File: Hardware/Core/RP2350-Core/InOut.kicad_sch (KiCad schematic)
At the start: 20 parts, among them CN10 PR5L4015-5P-C-F, CN11 PR5L4015-5P-C-F, CN7 PR5L4015-5P-C-F, CN8 PR5L4015-5P-C-F, CN9 PR5L4015-5P-C-F, J1 Conn_01x10_Socket, J2 Conn_01x10_Socket, J5 Conn_01x10_Socket, J6 Conn_01x10_Socket, J9 Conn_01x10_Socket, U35 PR5L5015-5P-C-H, U36 PR5L5015-5P-C-H, U37 PR5L5015-5P-C-H, U38 PR5L5015-5P-C-H, U39 PR5L5015-5P-C-H

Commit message: Verison RP2350 with arduino header support
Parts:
- removed J1, J2, J5, J6: Conn_01x10_Socket, Connector_PinHeader_2.54mm:PinHeader_2x10_P2.54mm_Vertical, symbol Connector:Conn_01x10_Socket
- J9: footprint Connector_PinHeader_2.54mm:PinHeader_2x10_P2.54mm_Vertical -> Connector_PinHeader_2.54mm:PinHeader_2x05_P2.54mm_Vertical
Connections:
- net ADC4_GPIO44 is gone; now on net SCL_ALT: A1.13 (SDA/A4)
- net ADC5_GPIO45 is gone; now on net SDA_ALT: A1.14 (SCL/A5)
- net GPIO25 is gone; now on net GPIO20: A1.24 (D9)
- net GPIO26 is gone; now on net GPIO21: A1.25 (D10)
- net GPIO27 is gone; now on net GPIO22: A1.26 (D11)
- net GPIO28 is gone; now on net GPIO23: A1.27 (D12)
- net GPIO29 is gone; now on net GPIO24: A1.28 (D13)
- net GPIO13: now also A1.19 (D4)
- net GPIO14: now also A1.20 (D5)
- net GPIO15: now also A1.21 (D6)
- net GPIO18: now also A1.22 (D7); no longer A1.17 (D2)
- net GPIO19: now also A1.23 (D8); no longer A1.18 (D3)
- net GPIO2: now also A1.17 (D2)
- net GPIO20: no longer A1.19 (D4)
- net GPIO21: no longer A1.20 (D5)
- net GPIO22: no longer A1.21 (D6)
- net GPIO23: no longer A1.22 (D7)
- net GPIO24: no longer A1.23 (D8)
- net GPIO4: now also A1.18 (D3)
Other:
- note added: "EXP HiSpeed"
- note removed: "EXP"
- moved on the sheet: J9

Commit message: Connectors connection improvements
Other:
- note added: "Only for RP235X-B"
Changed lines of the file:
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@@
+		)
+	)
+	(text "Only for RP235X-B"
+		(exclude_from_sim no)
+		(at 256.54 111.76 0)
+		(effects
+			(font
+				(size 2.54 2.54)
+			)
 		)
 	)

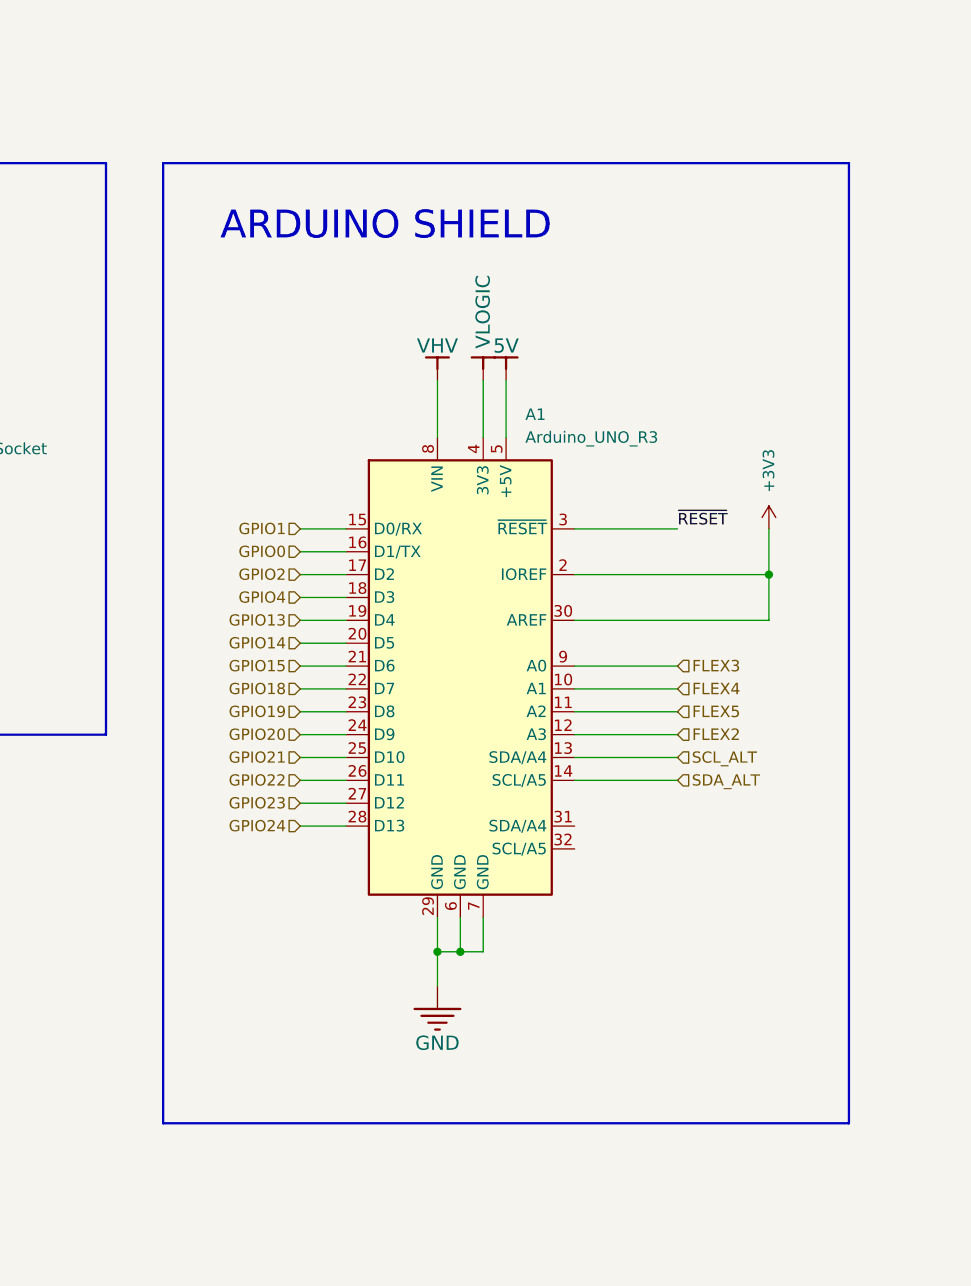
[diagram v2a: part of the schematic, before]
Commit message: Added ADC TI ADS1115IDGSR to match arduino pinout and function and isolate arduino connections from spaghetti bus
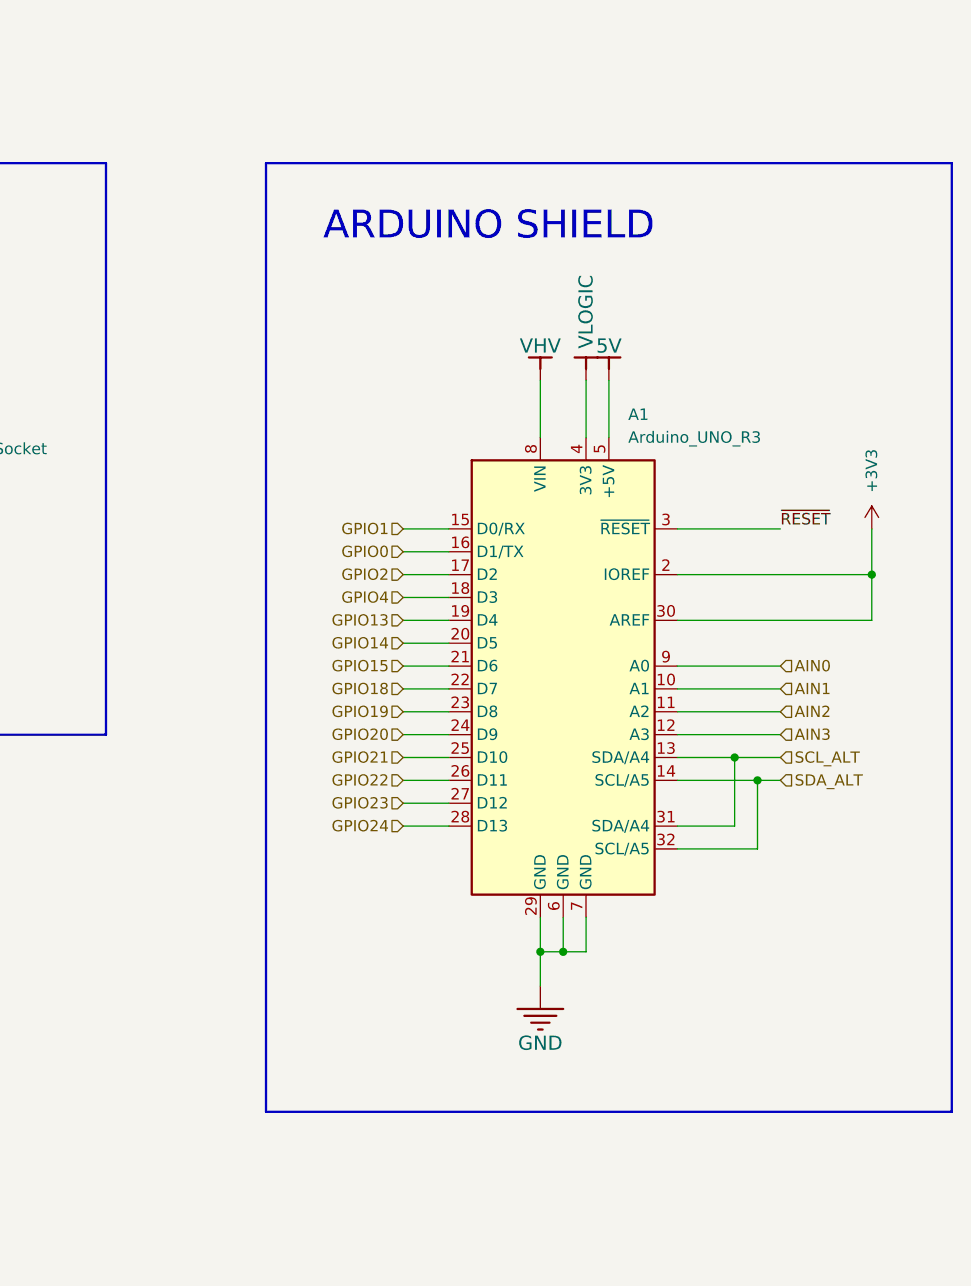
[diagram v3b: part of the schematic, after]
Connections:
- net FLEX2: no longer A1.12 (A3)
- net FLEX3: no longer A1.9 (A0)
- net FLEX4: no longer A1.10 (A1)
- net FLEX5: no longer A1.11 (A2)
- net SCL_ALT: now also A1.31 (SDA/A4)
- net SDA_ALT: now also A1.32 (SCL/A5)
- new net AIN0: A1.9 (A0)
- new net AIN1: A1.10 (A1)
- new net AIN2: A1.11 (A2)
- new net AIN3: A1.12 (A3)
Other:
- moved on the sheet: A1

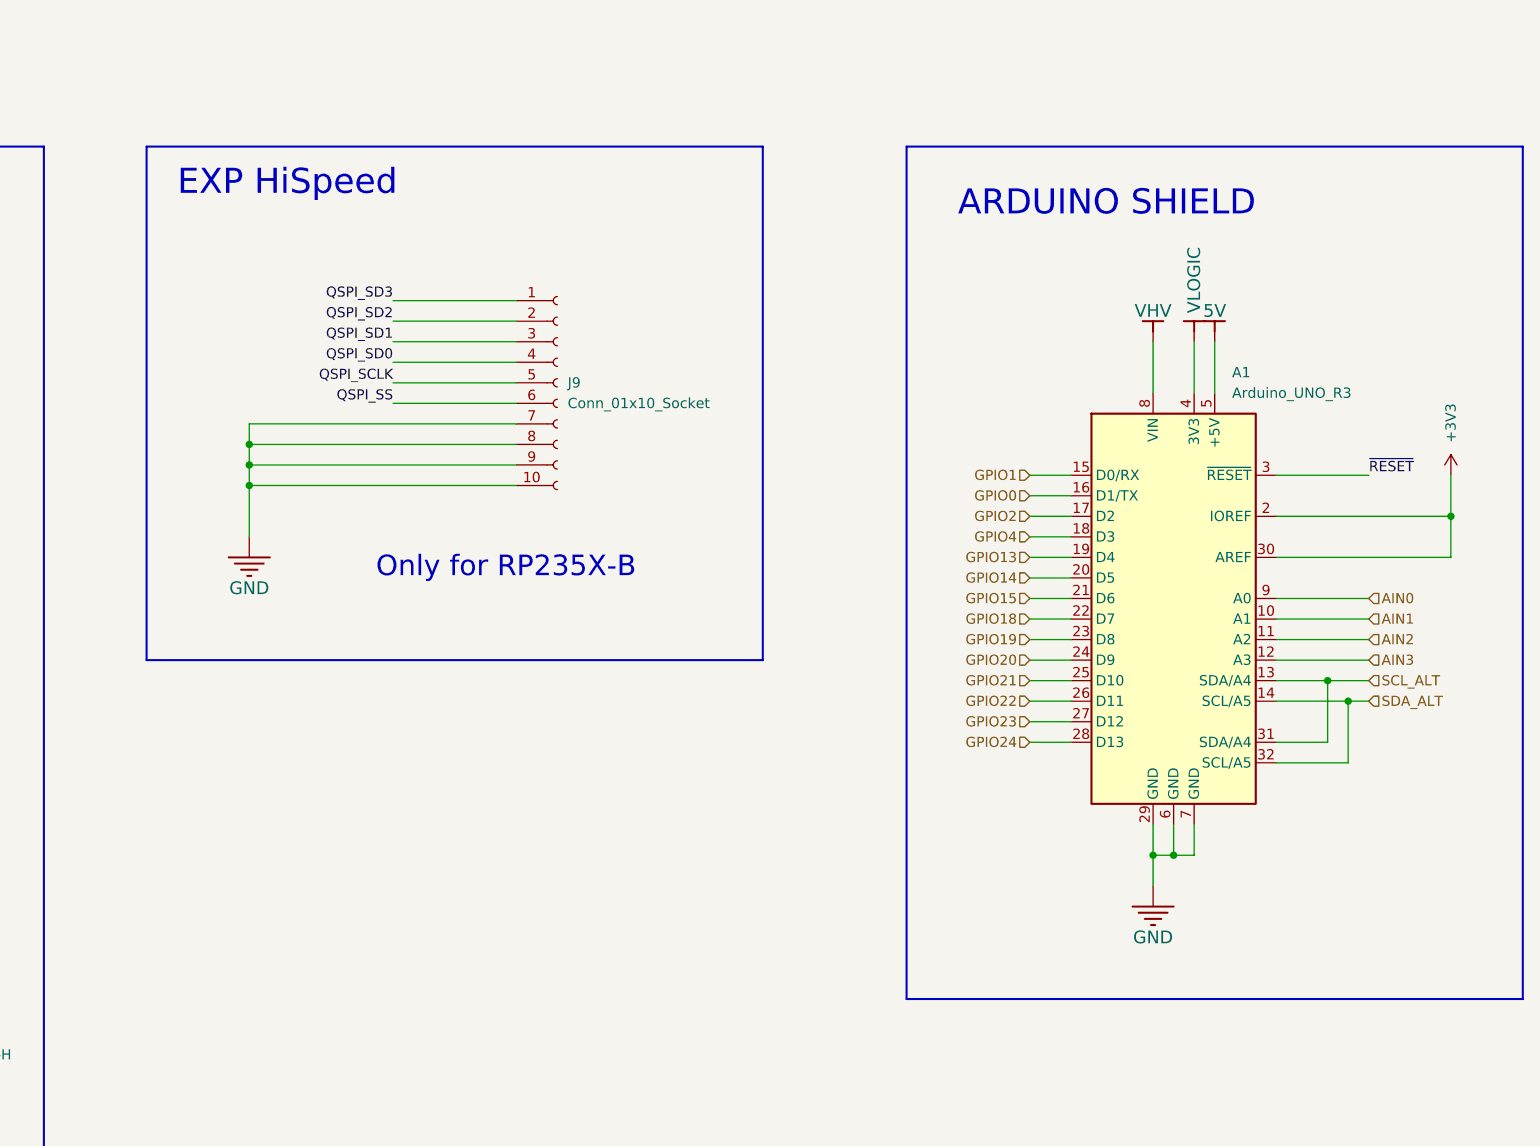
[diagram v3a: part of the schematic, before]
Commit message: Placed footprints RP235x
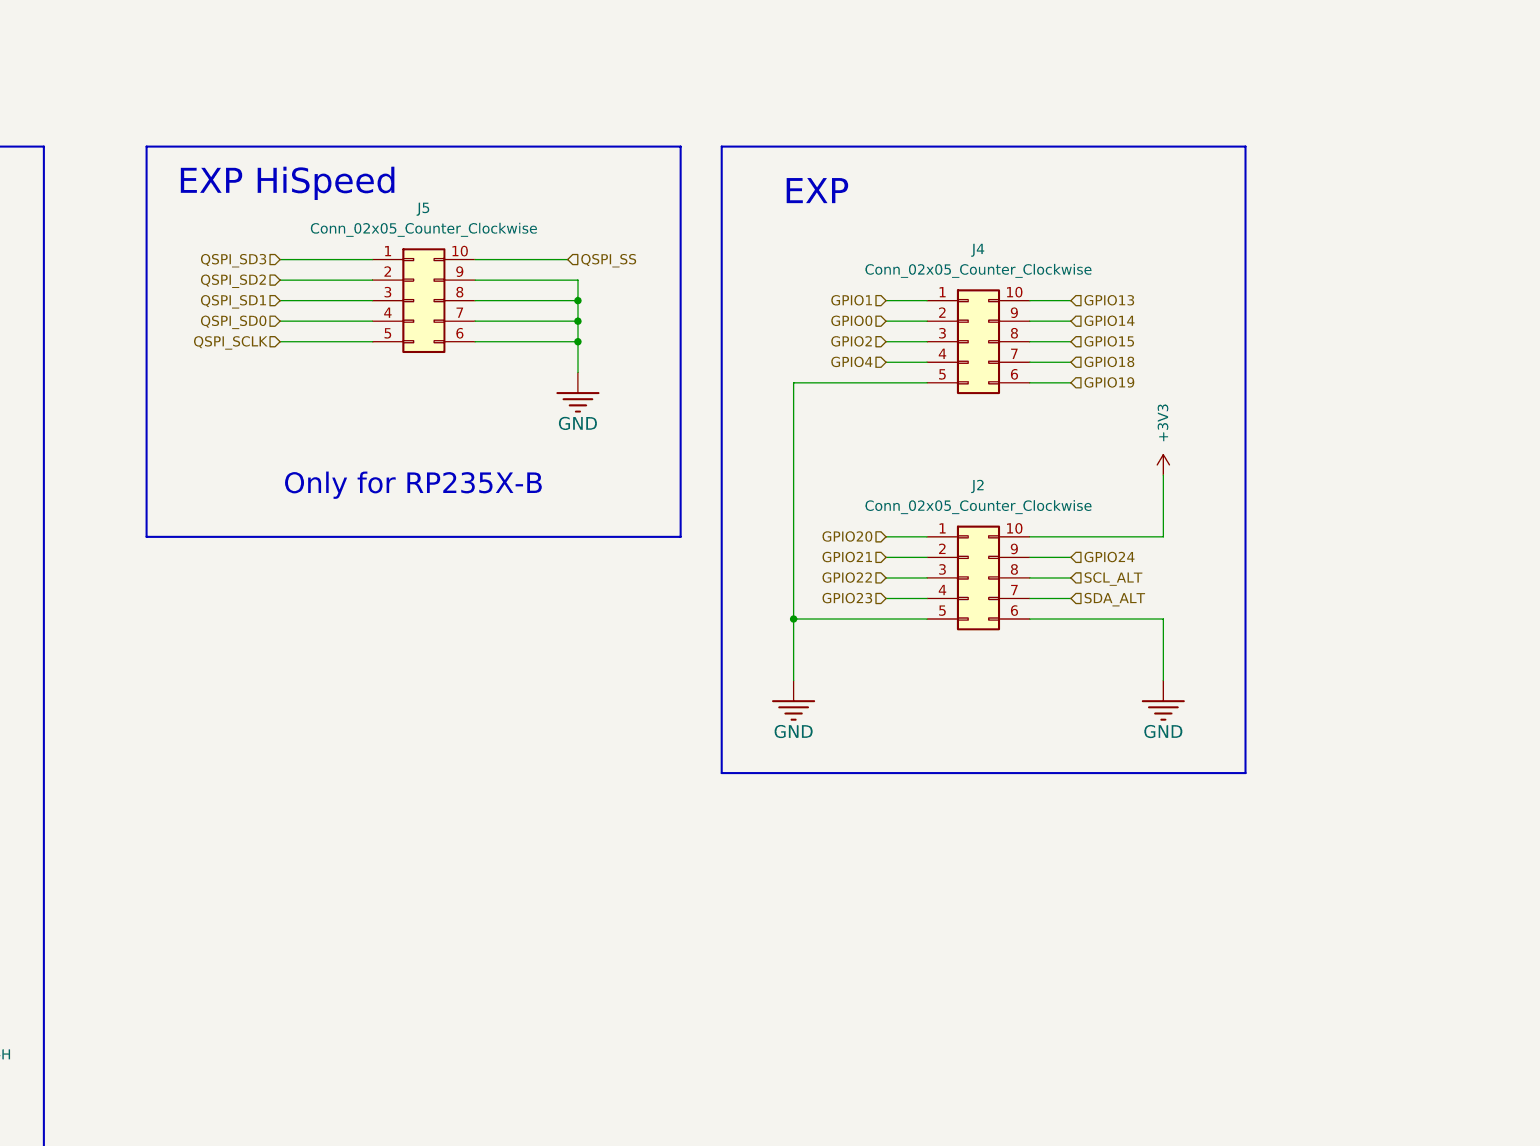
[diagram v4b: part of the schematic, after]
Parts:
- removed A1: Arduino_UNO_R3, Module:Arduino_UNO_R3, symbol MCU_Module:Arduino_UNO_R3
- removed J9: Conn_01x10_Socket, Connector_PinHeader_2.54mm:PinHeader_2x05_P2.54mm_Vertical, symbol Connector:Conn_01x10_Socket
- added J2, J4, J5: Conn_02x05_Counter_Clockwise, Connector_PinSocket_2.54mm:PinSocket_2x05_P2.54mm_Vertical, symbol Connector_Generic:Conn_02x05_Counter_Clockwise
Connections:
- net +3V3: now also J2.10 (Pin_10)
- net GND: now also J2.5 (Pin_5), J2.6 (Pin_6), J4.5 (Pin_5), J5.6 (Pin_6), J5.7 (Pin_7), J5.8 (Pin_8), J5.9 (Pin_9)
- net GPIO0: now also J4.2 (Pin_2)
- net GPIO1: now also J4.1 (Pin_1)
- net GPIO13: now also J4.10 (Pin_10)
- net GPIO14: now also J4.9 (Pin_9)
- net GPIO15: now also J4.8 (Pin_8)
- net GPIO18: now also J4.7 (Pin_7)
- net GPIO19: now also J4.6 (Pin_6)
- net GPIO2: now also J4.3 (Pin_3)
- net GPIO20: now also J2.1 (Pin_1)
- net GPIO21: now also J2.2 (Pin_2)
- net GPIO22: now also J2.3 (Pin_3)
- net GPIO23: now also J2.4 (Pin_4)
- net GPIO24: now also J2.9 (Pin_9)
- net GPIO4: now also J4.4 (Pin_4)
- net QSPI_SCLK: now also J5.5 (Pin_5)
- net QSPI_SD0: now also J5.4 (Pin_4)
- net QSPI_SD1: now also J5.3 (Pin_3)
- net QSPI_SD2: now also J5.2 (Pin_2)
- net QSPI_SD3: now also J5.1 (Pin_1)
- net QSPI_SS: now also J5.10 (Pin_10)
- net SCL_ALT: now also J2.8 (Pin_8)
- net SDA_ALT: now also J2.7 (Pin_7)
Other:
- note added: "EXP"
- note removed: "ARDUINO SHIELD"

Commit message: Routing core started
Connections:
- net GND: now also J5.2 (Pin_2), J5.5 (Pin_5); no longer J5.6 (Pin_6), J5.8 (Pin_8)
- net GPIO0: now also J4.10 (Pin_10); no longer J4.2 (Pin_2)
- net GPIO1: now also J4.8 (Pin_8); no longer J4.1 (Pin_1)
- net GPIO13: now also J4.3 (Pin_3); no longer J4.10 (Pin_10)
- net GPIO14: now also J4.2 (Pin_2); no longer J4.9 (Pin_9)
- net GPIO15: now also J4.1 (Pin_1); no longer J4.8 (Pin_8)
- net GPIO19: now also J4.9 (Pin_9); no longer J4.6 (Pin_6)
- net GPIO2: now also J4.6 (Pin_6); no longer J4.3 (Pin_3)
- net GPIO20: now also J2.4 (Pin_4); no longer J2.1 (Pin_1)
- net GPIO22: now also J2.1 (Pin_1); no longer J2.3 (Pin_3)
- net GPIO23: now also J2.3 (Pin_3); no longer J2.4 (Pin_4)
- net QSPI_SCLK: now also J5.3 (Pin_3); no longer J5.5 (Pin_5)
- net QSPI_SD0: now also J5.1 (Pin_1); no longer J5.4 (Pin_4)
- net QSPI_SD1: now also J5.8 (Pin_8); no longer J5.3 (Pin_3)
- net QSPI_SD2: now also J5.6 (Pin_6); no longer J5.2 (Pin_2)
- net QSPI_SD3: now also J5.4 (Pin_4); no longer J5.1 (Pin_1)

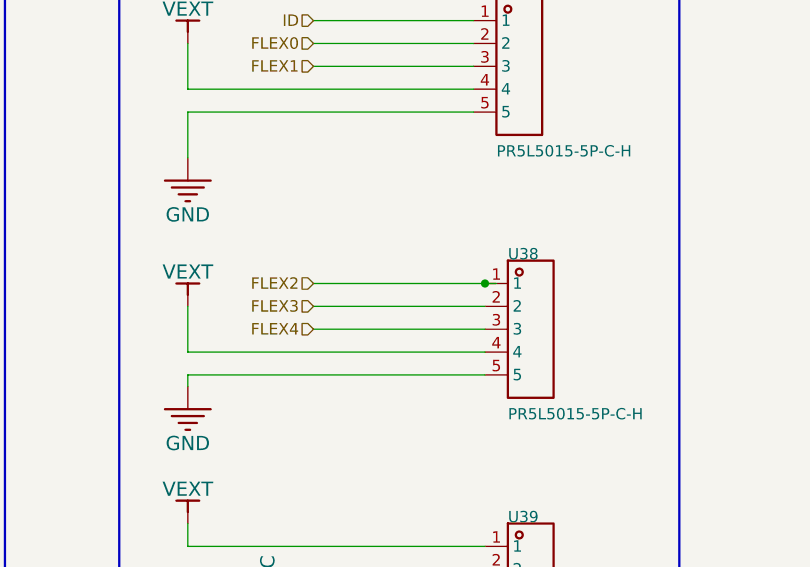
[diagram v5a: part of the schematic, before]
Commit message: RP235X Layout complete
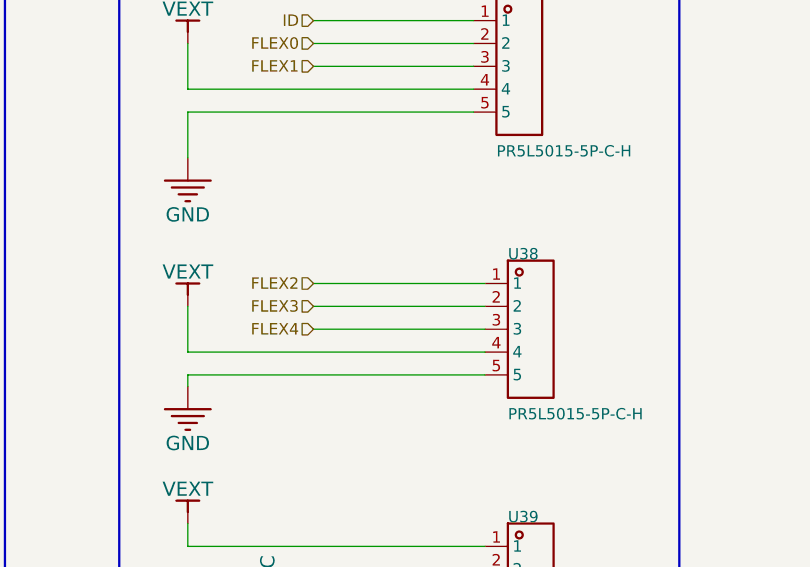
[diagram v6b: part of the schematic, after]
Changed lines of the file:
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@@
-	)
-	(junction
-		(at 177.8 157.48)
-		(diameter 0)
-		(color 0 0 0 0)
 	)
 	(junction
@@
 	(wire
 		(pts
-			(xy 177.8 157.48) (xy 179.07 157.48)
-		)
-		(stroke
-			(width 0)
-			(type default)
-		)
-	)
-	(wire
-		(pts
 			(xy 326.39 88.9) (xy 321.31 88.9)
 		)
@@
 	(wire
 		(pts
+			(xy 158.75 157.48) (xy 177.8 157.48)
+		)
+		(stroke
+			(width 0)
+			(type default)
+		)
+	)
+	(wire
+		(pts
 			(xy 308.61 118.11) (xy 292.1 118.11)
 		)
@@
 		)
 		(stroke
-			(width 0)
-			(type default)
-		)
-	)
-	(wire
-		(pts
-			(xy 177.8 157.48) (xy 158.75 157.48)
-		)
-		(stroke
